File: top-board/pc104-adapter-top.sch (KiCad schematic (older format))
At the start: 12 parts, among them J1 Conn_01x13_Male, J10 SAMTEC-TSW-126-07-X-D, J2 Conn_01x13_Male, J3 Conn_01x13_Male, J4 Conn_01x13_Male, J5 Conn_01x13_Male, J6 Conn_01x13_Male, J7 Conn_01x13_Male, J8 Conn_01x13_Male, J9 SAMTEC-TSW-126-07-X-D

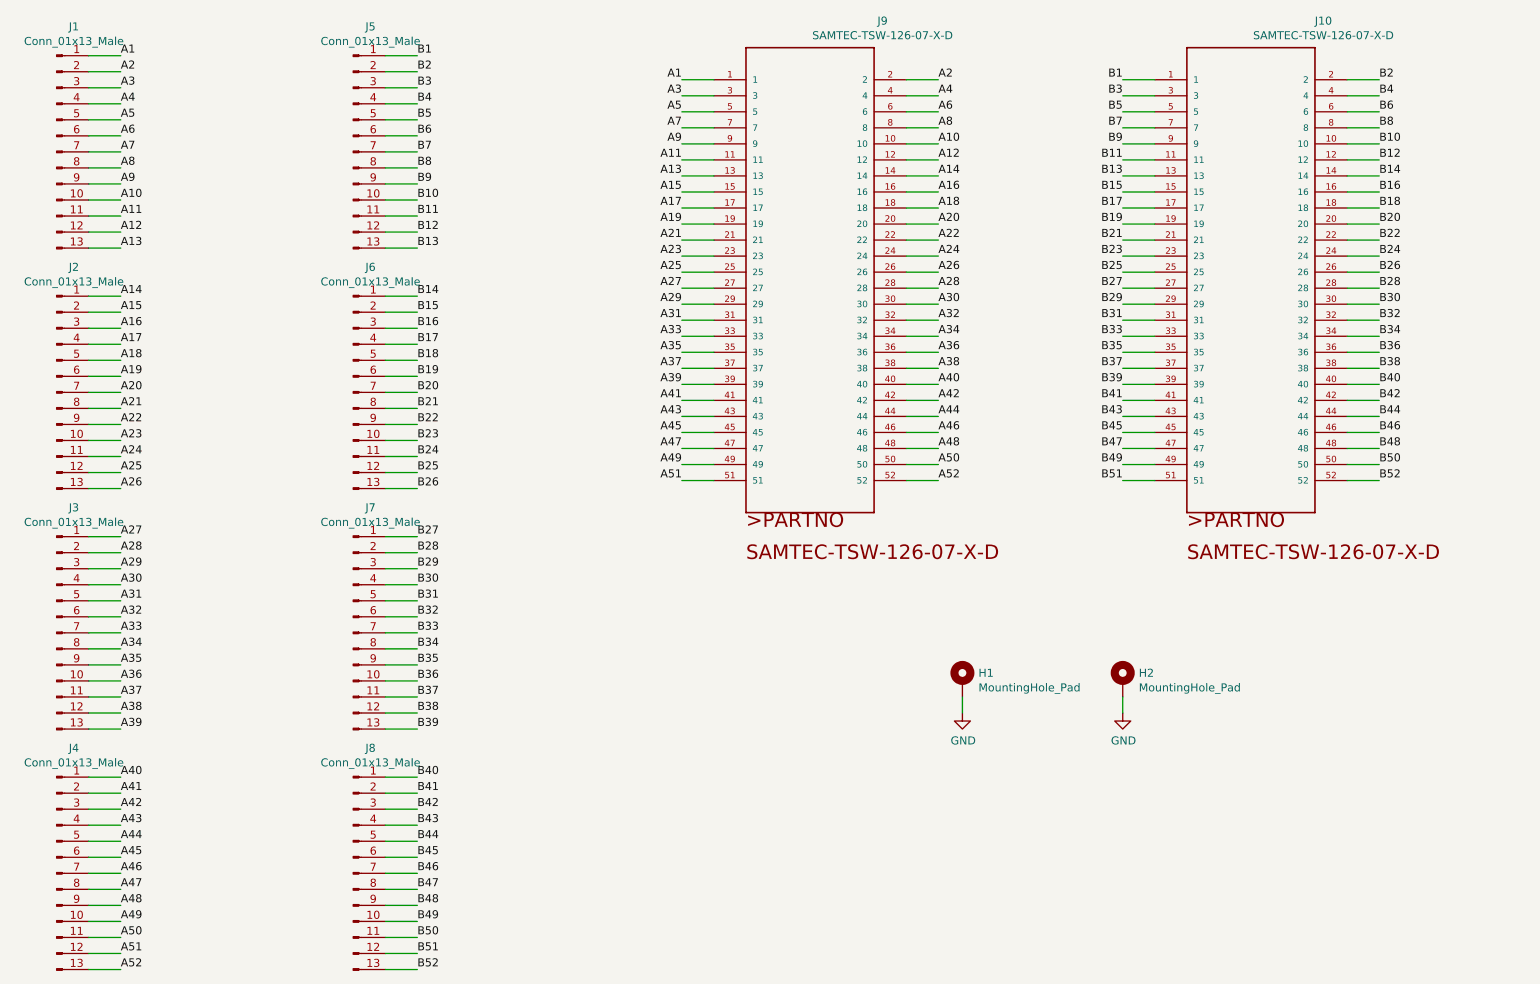
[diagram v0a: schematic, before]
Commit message: top-board: Schematic and PCB layout #7
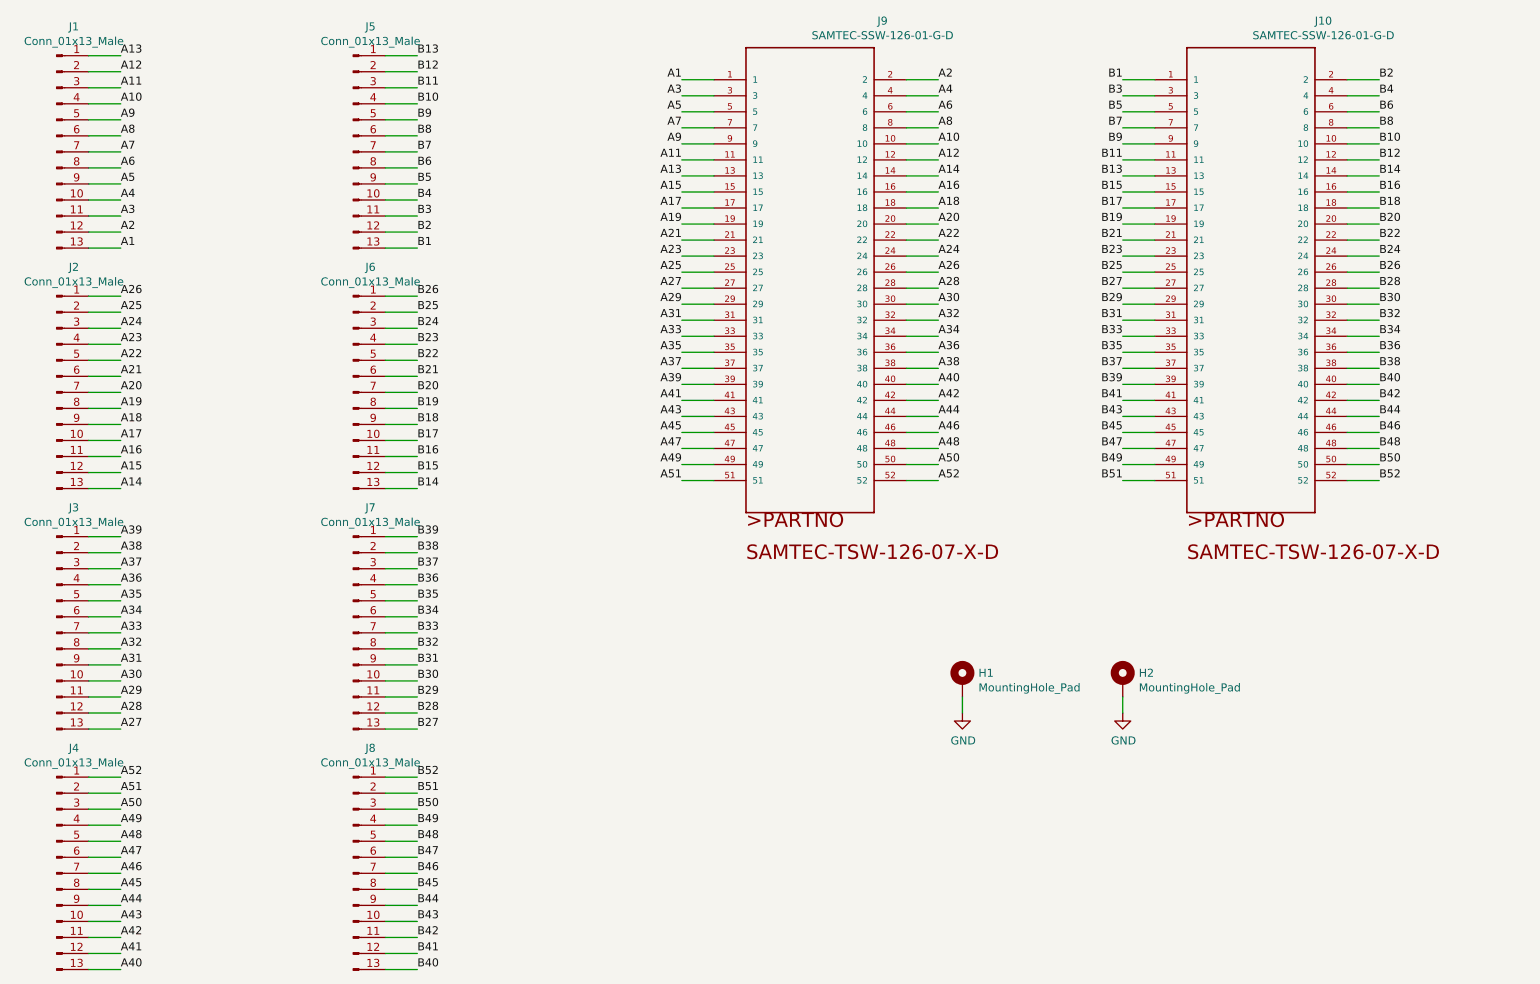
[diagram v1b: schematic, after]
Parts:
- J10, J9: value SAMTEC-TSW-126-07-X-D -> SAMTEC-SSW-126-01-G-D
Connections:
- net A1: now also J1.13 (Pin_13); no longer J1.1 (Pin_1)
- net A10: now also J1.4 (Pin_4); no longer J1.10 (Pin_10)
- net A11: now also J1.3 (Pin_3); no longer J1.11 (Pin_11)
- net A12: now also J1.2 (Pin_2); no longer J1.12 (Pin_12)
- net A13: now also J1.1 (Pin_1); no longer J1.13 (Pin_13)
- net A14: now also J2.13 (Pin_13); no longer J2.1 (Pin_1)
- net A15: now also J2.12 (Pin_12); no longer J2.2 (Pin_2)
- net A16: now also J2.11 (Pin_11); no longer J2.3 (Pin_3)
- net A17: now also J2.10 (Pin_10); no longer J2.4 (Pin_4)
- net A18: now also J2.9 (Pin_9); no longer J2.5 (Pin_5)
- net A19: now also J2.8 (Pin_8); no longer J2.6 (Pin_6)
- net A2: now also J1.12 (Pin_12); no longer J1.2 (Pin_2)
- net A21: now also J2.6 (Pin_6); no longer J2.8 (Pin_8)
- net A22: now also J2.5 (Pin_5); no longer J2.9 (Pin_9)
- net A23: now also J2.4 (Pin_4); no longer J2.10 (Pin_10)
- net A24: now also J2.3 (Pin_3); no longer J2.11 (Pin_11)
- net A25: now also J2.2 (Pin_2); no longer J2.12 (Pin_12)
- net A26: now also J2.1 (Pin_1); no longer J2.13 (Pin_13)
- net A27: now also J3.13 (Pin_13); no longer J3.1 (Pin_1)
- net A28: now also J3.12 (Pin_12); no longer J3.2 (Pin_2)
- net A29: now also J3.11 (Pin_11); no longer J3.3 (Pin_3)
- net A3: now also J1.11 (Pin_11); no longer J1.3 (Pin_3)
- net A30: now also J3.10 (Pin_10); no longer J3.4 (Pin_4)
- net A31: now also J3.9 (Pin_9); no longer J3.5 (Pin_5)
- net A32: now also J3.8 (Pin_8); no longer J3.6 (Pin_6)
- net A34: now also J3.6 (Pin_6); no longer J3.8 (Pin_8)
- net A35: now also J3.5 (Pin_5); no longer J3.9 (Pin_9)
- net A36: now also J3.4 (Pin_4); no longer J3.10 (Pin_10)
- net A37: now also J3.3 (Pin_3); no longer J3.11 (Pin_11)
- net A38: now also J3.2 (Pin_2); no longer J3.12 (Pin_12)
- net A39: now also J3.1 (Pin_1); no longer J3.13 (Pin_13)
- net A4: now also J1.10 (Pin_10); no longer J1.4 (Pin_4)
- net A40: now also J4.13 (Pin_13); no longer J4.1 (Pin_1)
- net A41: now also J4.12 (Pin_12); no longer J4.2 (Pin_2)
- net A42: now also J4.11 (Pin_11); no longer J4.3 (Pin_3)
- net A43: now also J4.10 (Pin_10); no longer J4.4 (Pin_4)
- net A44: now also J4.9 (Pin_9); no longer J4.5 (Pin_5)
- net A45: now also J4.8 (Pin_8); no longer J4.6 (Pin_6)
- net A47: now also J4.6 (Pin_6); no longer J4.8 (Pin_8)
- net A48: now also J4.5 (Pin_5); no longer J4.9 (Pin_9)
- net A49: now also J4.4 (Pin_4); no longer J4.10 (Pin_10)
- net A5: now also J1.9 (Pin_9); no longer J1.5 (Pin_5)
- net A50: now also J4.3 (Pin_3); no longer J4.11 (Pin_11)
- net A51: now also J4.2 (Pin_2); no longer J4.12 (Pin_12)
- net A52: now also J4.1 (Pin_1); no longer J4.13 (Pin_13)
- net A6: now also J1.8 (Pin_8); no longer J1.6 (Pin_6)
- net A8: now also J1.6 (Pin_6); no longer J1.8 (Pin_8)
- net A9: now also J1.5 (Pin_5); no longer J1.9 (Pin_9)
- net B1: now also J5.13 (Pin_13); no longer J5.1 (Pin_1)
- net B10: now also J5.4 (Pin_4); no longer J5.10 (Pin_10)
- net B11: now also J5.3 (Pin_3); no longer J5.11 (Pin_11)
- net B12: now also J5.2 (Pin_2); no longer J5.12 (Pin_12)
- net B13: now also J5.1 (Pin_1); no longer J5.13 (Pin_13)
- net B14: now also J6.13 (Pin_13); no longer J6.1 (Pin_1)
- net B15: now also J6.12 (Pin_12); no longer J6.2 (Pin_2)
- net B16: now also J6.11 (Pin_11); no longer J6.3 (Pin_3)
- net B17: now also J6.10 (Pin_10); no longer J6.4 (Pin_4)
- net B18: now also J6.9 (Pin_9); no longer J6.5 (Pin_5)
- net B19: now also J6.8 (Pin_8); no longer J6.6 (Pin_6)
- net B2: now also J5.12 (Pin_12); no longer J5.2 (Pin_2)
- net B21: now also J6.6 (Pin_6); no longer J6.8 (Pin_8)
- net B22: now also J6.5 (Pin_5); no longer J6.9 (Pin_9)
- net B23: now also J6.4 (Pin_4); no longer J6.10 (Pin_10)
- net B24: now also J6.3 (Pin_3); no longer J6.11 (Pin_11)
- net B25: now also J6.2 (Pin_2); no longer J6.12 (Pin_12)
- net B26: now also J6.1 (Pin_1); no longer J6.13 (Pin_13)
- net B27: now also J7.13 (Pin_13); no longer J7.1 (Pin_1)
- net B28: now also J7.12 (Pin_12); no longer J7.2 (Pin_2)
- net B29: now also J7.11 (Pin_11); no longer J7.3 (Pin_3)
- net B3: now also J5.11 (Pin_11); no longer J5.3 (Pin_3)
- net B30: now also J7.10 (Pin_10); no longer J7.4 (Pin_4)
- net B31: now also J7.9 (Pin_9); no longer J7.5 (Pin_5)
- net B32: now also J7.8 (Pin_8); no longer J7.6 (Pin_6)
- net B34: now also J7.6 (Pin_6); no longer J7.8 (Pin_8)
- net B35: now also J7.5 (Pin_5); no longer J7.9 (Pin_9)
- net B36: now also J7.4 (Pin_4); no longer J7.10 (Pin_10)
- net B37: now also J7.3 (Pin_3); no longer J7.11 (Pin_11)
- net B38: now also J7.2 (Pin_2); no longer J7.12 (Pin_12)
- net B39: now also J7.1 (Pin_1); no longer J7.13 (Pin_13)
- net B4: now also J5.10 (Pin_10); no longer J5.4 (Pin_4)
- net B40: now also J8.13 (Pin_13); no longer J8.1 (Pin_1)
- net B41: now also J8.12 (Pin_12); no longer J8.2 (Pin_2)
- net B42: now also J8.11 (Pin_11); no longer J8.3 (Pin_3)
- net B43: now also J8.10 (Pin_10); no longer J8.4 (Pin_4)
- net B44: now also J8.9 (Pin_9); no longer J8.5 (Pin_5)
- net B45: now also J8.8 (Pin_8); no longer J8.6 (Pin_6)
- net B47: now also J8.6 (Pin_6); no longer J8.8 (Pin_8)
- net B48: now also J8.5 (Pin_5); no longer J8.9 (Pin_9)
- net B49: now also J8.4 (Pin_4); no longer J8.10 (Pin_10)
- net B5: now also J5.9 (Pin_9); no longer J5.5 (Pin_5)
- net B50: now also J8.3 (Pin_3); no longer J8.11 (Pin_11)
- net B51: now also J8.2 (Pin_2); no longer J8.12 (Pin_12)
- net B52: now also J8.1 (Pin_1); no longer J8.13 (Pin_13)
- net B6: now also J5.8 (Pin_8); no longer J5.6 (Pin_6)
- net B8: now also J5.6 (Pin_6); no longer J5.8 (Pin_8)
- net B9: now also J5.5 (Pin_5); no longer J5.9 (Pin_9)

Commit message: top-board: Version 2.0 #13
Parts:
- added H3, H4: MountingHole_Pad, MountingHole:MountingHole_3.2mm_M3_ISO14580_Pad, symbol Mechanical:MountingHole_Pad
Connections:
- net GND: now also H3.1, H4.1
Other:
- moved on the sheet: H1, H2
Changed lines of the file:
@@
 L Mechanical:MountingHole_Pad H1
 U 1 1 5F59E490
-P 7450 5250
-F 0 "H1" H 7550 5299 50  0000 L CNN
-F 1 "MountingHole_Pad" H 7550 5208 50  0000 L CNN
-F 2 "MountingHole:MountingHole_3.2mm_M3_ISO14580_Pad" H 7450 5250 50  0001 C CNN
-F 3 "~" H 7450 5250 50  0001 C CNN
-	1    7450 5250
+P 6400 5300
+F 0 "H1" H 6500 5349 50  0000 L CNN
+F 1 "MountingHole_Pad" H 6500 5258 50  0000 L CNN
+F 2 "MountingHole:MountingHole_3.2mm_M3_ISO14580_Pad" H 6400 5300 50  0001 C CNN
+F 3 "~" H 6400 5300 50  0001 C CNN
+	1    6400 5300
 	1    0    0    -1
 $EndComp
@@
 L Mechanical:MountingHole_Pad H2
 U 1 1 5F5A173F
-P 8450 5250
-F 0 "H2" H 8550 5299 50  0000 L CNN
-F 1 "MountingHole_Pad" H 8550 5208 50  0000 L CNN
-F 2 "MountingHole:MountingHole_3.2mm_M3_ISO14580_Pad" H 8450 5250 50  0001 C CNN
-F 3 "~" H 8450 5250 50  0001 C CNN
-	1    8450 5250
+P 7400 5300
+F 0 "H2" H 7500 5349 50  0000 L CNN
+F 1 "MountingHole_Pad" H 7500 5258 50  0000 L CNN
+F 2 "MountingHole:MountingHole_3.2mm_M3_ISO14580_Pad" H 7400 5300 50  0001 C CNN
+F 3 "~" H 7400 5300 50  0001 C CNN
+	1    7400 5300
 	1    0    0    -1
 $EndComp
@@
 L power:GND #PWR01
 U 1 1 5F5D55CB
-P 7450 5450
-F 0 "#PWR01" H 7450 5200 50  0001 C CNN
-F 1 "GND" H 7455 5277 50  0000 C CNN
-F 2 "" H 7450 5450 50  0001 C CNN
-F 3 "" H 7450 5450 50  0001 C CNN
-	1    7450 5450
+P 6400 5500
+F 0 "#PWR01" H 6400 5250 50  0001 C CNN
+F 1 "GND" H 6405 5327 50  0000 C CNN
+F 2 "" H 6400 5500 50  0001 C CNN
+F 3 "" H 6400 5500 50  0001 C CNN
+	1    6400 5500
 	1    0    0    -1
 $EndComp
@@
 L power:GND #PWR02
 U 1 1 5F5D6345
-P 8450 5450
-F 0 "#PWR02" H 8450 5200 50  0001 C CNN
-F 1 "GND" H 8455 5277 50  0000 C CNN
-F 2 "" H 8450 5450 50  0001 C CNN
-F 3 "" H 8450 5450 50  0001 C CNN
-	1    8450 5450
-	1    0    0    -1
-$EndComp
-Wire Wire Line
-	7450 5450 7450 5350
-Wire Wire Line
-	8450 5450 8450 5350
+P 7400 5500
+F 0 "#PWR02" H 7400 5250 50  0001 C CNN
+F 1 "GND" H 7405 5327 50  0000 C CNN
+F 2 "" H 7400 5500 50  0001 C CNN
+F 3 "" H 7400 5500 50  0001 C CNN
+	1    7400 5500
+	1    0    0    -1
+$EndComp
+Wire Wire Line
+	6400 5500 6400 5400
+Wire Wire Line
+	7400 5500 7400 5400
 Wire Wire Line
 	2200 2550 2000 2550
@@
 	1    0    0    -1
 $EndComp
+$Comp
+L Mechanical:MountingHole_Pad H3
+U 1 1 5F352380
+P 8400 5300
+F 0 "H3" H 8500 5349 50  0000 L CNN
+F 1 "MountingHole_Pad" H 8500 5258 50  0000 L CNN
+F 2 "MountingHole:MountingHole_3.2mm_M3_ISO14580_Pad" H 8400 5300 50  0001 C CNN
+F 3 "~" H 8400 5300 50  0001 C CNN
+	1    8400 5300
+	1    0    0    -1
+$EndComp
+$Comp
+L Mechanical:MountingHole_Pad H4
+U 1 1 5F352386
+P 9400 5300
+F 0 "H4" H 9500 5349 50  0000 L CNN
+F 1 "MountingHole_Pad" H 9500 5258 50  0000 L CNN
+F 2 "MountingHole:MountingHole_3.2mm_M3_ISO14580_Pad" H 9400 5300 50  0001 C CNN
+F 3 "~" H 9400 5300 50  0001 C CNN
+	1    9400 5300
+	1    0    0    -1
+$EndComp
+$Comp
+L power:GND #PWR0101
+U 1 1 5F35238C
+P 8400 5500
+F 0 "#PWR0101" H 8400 5250 50  0001 C CNN
+F 1 "GND" H 8405 5327 50  0000 C CNN
+F 2 "" H 8400 5500 50  0001 C CNN
+F 3 "" H 8400 5500 50  0001 C CNN
+	1    8400 5500
+	1    0    0    -1
+$EndComp
+$Comp
+L power:GND #PWR0102
+U 1 1 5F352392
+P 9400 5500
+F 0 "#PWR0102" H 9400 5250 50  0001 C CNN
+F 1 "GND" H 9405 5327 50  0000 C CNN
+F 2 "" H 9400 5500 50  0001 C CNN
+F 3 "" H 9400 5500 50  0001 C CNN
+	1    9400 5500
+	1    0    0    -1
+$EndComp
+Wire Wire Line
+	8400 5500 8400 5400
+Wire Wire Line
+	9400 5500 9400 5400
 $EndSCHEMATC
